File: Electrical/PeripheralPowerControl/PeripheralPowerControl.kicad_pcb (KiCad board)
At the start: 2 copper layers, 40 x 63 mm, 6 parts, among them J1 Conn_01x03, J2 Screw_Terminal_01x02, J3 Conn_01x03

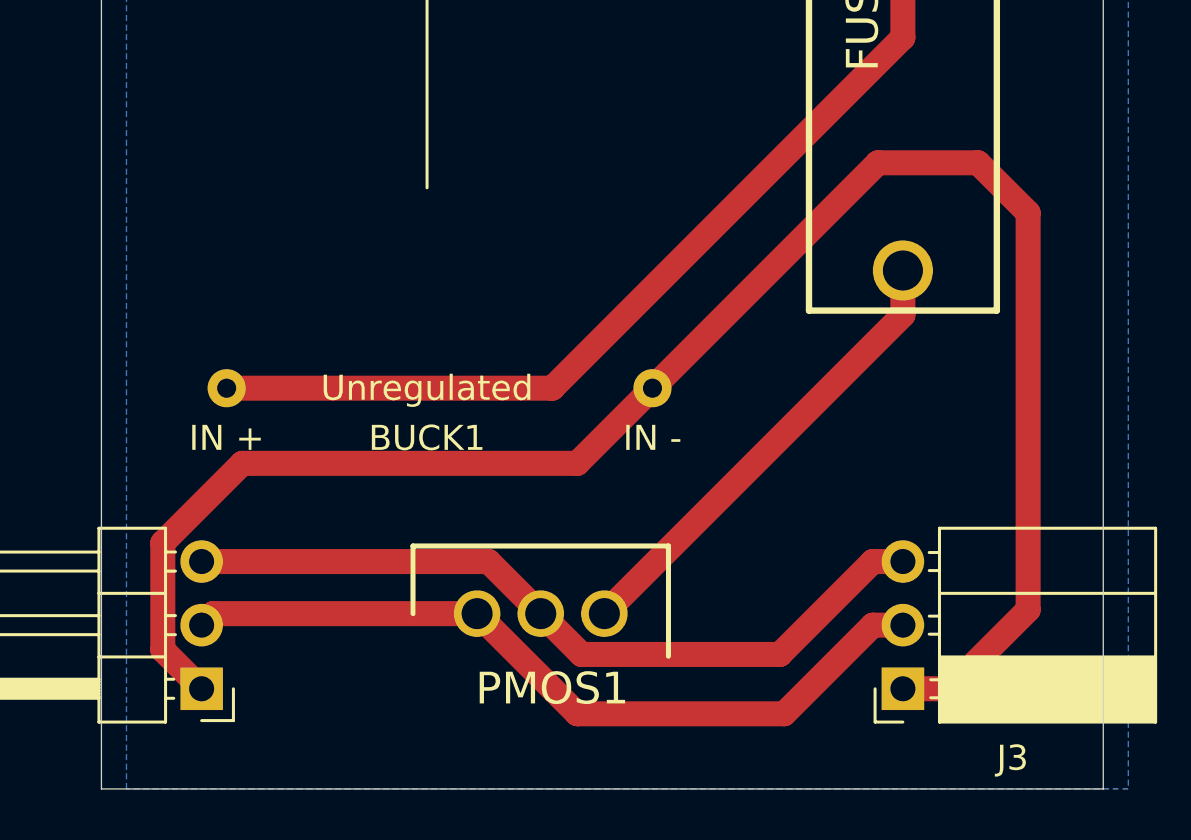
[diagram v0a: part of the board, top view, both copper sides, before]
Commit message: Adds ground plane to the peripheral board
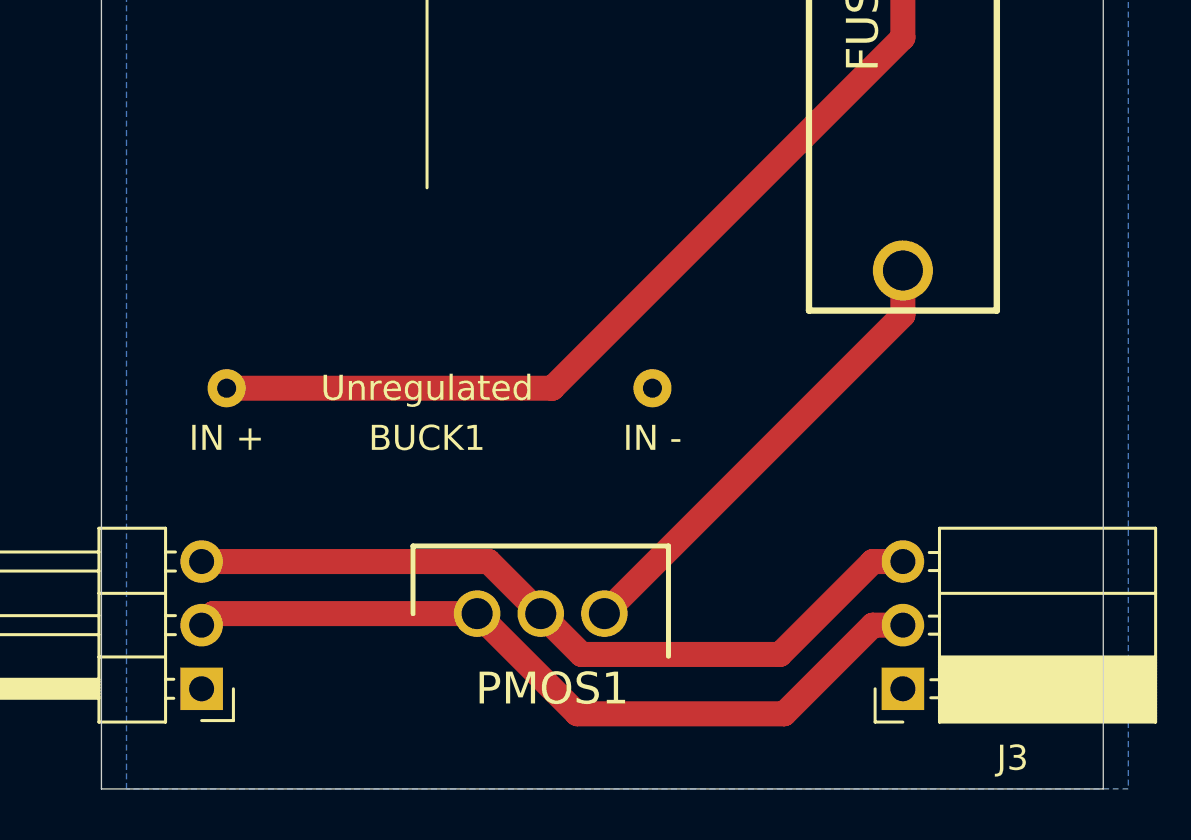
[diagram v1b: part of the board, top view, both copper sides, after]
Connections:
- net Net-(BUCK1-Pad1) renamed GND
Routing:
- net GND: track 70.3 -> 0.00 mm
- added copper zone on B.Cu, net GND
- removed copper zone on B.Cu, net (none)
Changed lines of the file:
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@@
     (thickness 1.6)
     (drawings 6)
-    (tracks 34)
+    (tracks 23)
     (zones 0)
     (modules 6)
@@
   (net 2 "Net-(BUCK1-Pad3)")
   (net 3 "Net-(BUCK1-Pad2)")
-  (net 4 "Net-(BUCK1-Pad1)")
-  (net 5 "Net-(FUSE1-Pad1)")
-  (net 6 "Net-(J1-Pad3)")
-  (net 7 "Net-(J1-Pad2)")
+  (net 4 "Net-(FUSE1-Pad1)")
+  (net 5 "Net-(J1-Pad3)")
+  (net 6 "Net-(J1-Pad2)")
+  (net 7 GND)
   (net_class Default "This is the default net class."
     (clearance 0.2)
@@
     (uvia_dia 0.3)
     (uvia_drill 0.1)
-    (add_net "Net-(BUCK1-Pad1)")
+    (add_net GND)
     (add_net "Net-(BUCK1-Pad2)")
     (add_net "Net-(BUCK1-Pad3)")
@@
     )
     (pad 3 thru_hole circle (at 5.08 0) (size 1.86 1.86) (drill 1.24) (layers *.Cu *.Mask)
-      (net 5 "Net-(FUSE1-Pad1)"))
+      (net 4 "Net-(FUSE1-Pad1)"))
     (pad 2 thru_hole circle (at 2.54 0) (size 1.86 1.86) (drill 1.24) (layers *.Cu *.Mask)
-      (net 6 "Net-(J1-Pad3)"))
+      (net 5 "Net-(J1-Pad3)"))
     (pad 1 thru_hole circle (at 0 0) (size 1.86 1.86) (drill 1.24) (layers *.Cu *.Mask)
-      (net 7 "Net-(J1-Pad2)"))
+      (net 6 "Net-(J1-Pad2)"))
     (model "C:\\Users\\jklei\\KiCad Libs\\SamacSys_Parts.3dshapes\\IPP120P04P4L03AKSA1.stp"
       (at (xyz 0 0 0))
@@
     (fp_line (start -10.03 -1.27) (end -2.49 -1.27) (layer F.Fab) (width 0.1))
     (pad 3 thru_hole oval (at 0 5.08 180) (size 1.7 1.7) (drill 1) (layers *.Cu *.Mask)
-      (net 6 "Net-(J1-Pad3)"))
+      (net 5 "Net-(J1-Pad3)"))
     (pad 2 thru_hole oval (at 0 2.54 180) (size 1.7 1.7) (drill 1) (layers *.Cu *.Mask)
-      (net 7 "Net-(J1-Pad2)"))
+      (net 6 "Net-(J1-Pad2)"))
     (pad 1 thru_hole rect (at 0 0 180) (size 1.7 1.7) (drill 1) (layers *.Cu *.Mask)
-      (net 4 "Net-(BUCK1-Pad1)"))
+      (net 7 GND))
     (model ${KISYS3DMOD}/Connector_PinSocket_2.54mm.3dshapes/PinSocket_1x03_P2.54mm_Horizontal.wrl
       (at (xyz 0 0 0))
@@
     (fp_line (start 2.135 -1.27) (end 4.04 -1.27) (layer F.Fab) (width 0.1))
     (pad 3 thru_hole oval (at 0 5.08 180) (size 1.7 1.7) (drill 1) (layers *.Cu *.Mask)
-      (net 6 "Net-(J1-Pad3)"))
+      (net 5 "Net-(J1-Pad3)"))
     (pad 2 thru_hole oval (at 0 2.54 180) (size 1.7 1.7) (drill 1) (layers *.Cu *.Mask)
-      (net 7 "Net-(J1-Pad2)"))
+      (net 6 "Net-(J1-Pad2)"))
     (pad 1 thru_hole rect (at 0 0 180) (size 1.7 1.7) (drill 1) (layers *.Cu *.Mask)
-      (net 4 "Net-(BUCK1-Pad1)"))
+      (net 7 GND))
     (model ${KISYS3DMOD}/Connector_PinHeader_2.54mm.3dshapes/PinHeader_1x03_P2.54mm_Horizontal.wrl
       (at (xyz 0 0 0))
@@
       (net 3 "Net-(BUCK1-Pad2)"))
     (pad 1 thru_hole circle (at -11.3 0 90) (size 2.4 2.4) (drill 1.6) (layers *.Cu *.Mask)
-      (net 5 "Net-(FUSE1-Pad1)"))
+      (net 4 "Net-(FUSE1-Pad1)"))
   )
   (module SCR_KiCAD_Lib:LM2596 (layer F.Cu)
@@
       (net 3 "Net-(BUCK1-Pad2)"))
     (pad 1 thru_hole circle (at -10 3 180) (size 1.524 1.524) (drill 0.762) (layers *.Cu *.Mask)
-      (net 4 "Net-(BUCK1-Pad1)"))
+      (net 7 GND))
   )
   (gr_line (start 53 10) (end 53 73) (layer Edge.Cuts) (width 0.05))
@@
   (segment (start 31 57) (end 18 57) (width 1) (layer F.Cu) (net 3))
   (segment (start 45 43) (end 31 57) (width 1) (layer F.Cu) (net 3))
-  (segment (start 15.449999 67.449999) (end 17 69) (width 1) (layer F.Cu) (net 4))
-  (segment (start 15.449999 63.175999) (end 15.449999 67.449999) (width 1) (layer F.Cu) (net 4))
-  (segment (start 18.625998 60) (end 15.449999 63.175999) (width 1) (layer F.Cu) (net 4))
-  (segment (start 32 60) (end 18.625998 60) (width 1) (layer F.Cu) (net 4))
-  (segment (start 35 57) (end 32 60) (width 1) (layer F.Cu) (net 4))
-  (segment (start 46.85 69) (end 45 69) (width 1) (layer F.Cu) (net 4))
-  (segment (start 50 65.85) (end 46.85 69) (width 1) (layer F.Cu) (net 4))
-  (segment (start 50 50) (end 50 65.85) (width 1) (layer F.Cu) (net 4))
-  (segment (start 48 48) (end 50 50) (width 1) (layer F.Cu) (net 4))
-  (segment (start 44 48) (end 48 48) (width 1) (layer F.Cu) (net 4))
-  (segment (start 35 57) (end 44 48) (width 1) (layer F.Cu) (net 4))
-  (segment (start 45 54.08) (end 45 52.3) (width 1) (layer F.Cu) (net 5))
-  (segment (start 33.08 66) (end 45 54.08) (width 1) (layer F.Cu) (net 5))
-  (segment (start 28.46 63.92) (end 30.54 66) (width 1) (layer F.Cu) (net 6))
-  (segment (start 17 63.92) (end 28.46 63.92) (width 1) (layer F.Cu) (net 6))
-  (segment (start 43.797919 63.92) (end 45 63.92) (width 1) (layer F.Cu) (net 6))
-  (segment (start 40.087918 67.630001) (end 43.797919 63.92) (width 1) (layer F.Cu) (net 6))
-  (segment (start 32.170001 67.630001) (end 40.087918 67.630001) (width 1) (layer F.Cu) (net 6))
-  (segment (start 30.54 66) (end 32.170001 67.630001) (width 1) (layer F.Cu) (net 6))
-  (segment (start 17.46 66) (end 17 66.46) (width 1) (layer F.Cu) (net 7))
-  (segment (start 28 66) (end 17.46 66) (width 1) (layer F.Cu) (net 7))
-  (segment (start 32 70) (end 28 66) (width 1) (layer F.Cu) (net 7))
-  (segment (start 40.257919 70) (end 32 70) (width 1) (layer F.Cu) (net 7))
-  (segment (start 43.797919 66.46) (end 40.257919 70) (width 1) (layer F.Cu) (net 7))
-  (segment (start 45 66.46) (end 43.797919 66.46) (width 1) (layer F.Cu) (net 7))
-  (zone (net 0) (net_name "") (layer B.Cu) (hatch edge 0.508)
+  (segment (start 45 54.08) (end 45 52.3) (width 1) (layer F.Cu) (net 4))
+  (segment (start 33.08 66) (end 45 54.08) (width 1) (layer F.Cu) (net 4))
+  (segment (start 28.46 63.92) (end 30.54 66) (width 1) (layer F.Cu) (net 5))
+  (segment (start 17 63.92) (end 28.46 63.92) (width 1) (layer F.Cu) (net 5))
+  (segment (start 43.797919 63.92) (end 45 63.92) (width 1) (layer F.Cu) (net 5))
+  (segment (start 40.087918 67.630001) (end 43.797919 63.92) (width 1) (layer F.Cu) (net 5))
+  (segment (start 32.170001 67.630001) (end 40.087918 67.630001) (width 1) (layer F.Cu) (net 5))
+  (segment (start 30.54 66) (end 32.170001 67.630001) (width 1) (layer F.Cu) (net 5))
+  (segment (start 17.46 66) (end 17 66.46) (width 1) (layer F.Cu) (net 6))
+  (segment (start 28 66) (end 17.46 66) (width 1) (layer F.Cu) (net 6))
+  (segment (start 32 70) (end 28 66) (width 1) (layer F.Cu) (net 6))
+  (segment (start 40.257919 70) (end 32 70) (width 1) (layer F.Cu) (net 6))
+  (segment (start 43.797919 66.46) (end 40.257919 70) (width 1) (layer F.Cu) (net 6))
+  (segment (start 45 66.46) (end 43.797919 66.46) (width 1) (layer F.Cu) (net 6))
+  (zone (net 7) (net_name GND) (layer B.Cu) (hatch edge 0.508)
     (connect_pads (clearance 0.508))
     (min_thickness 0.254)

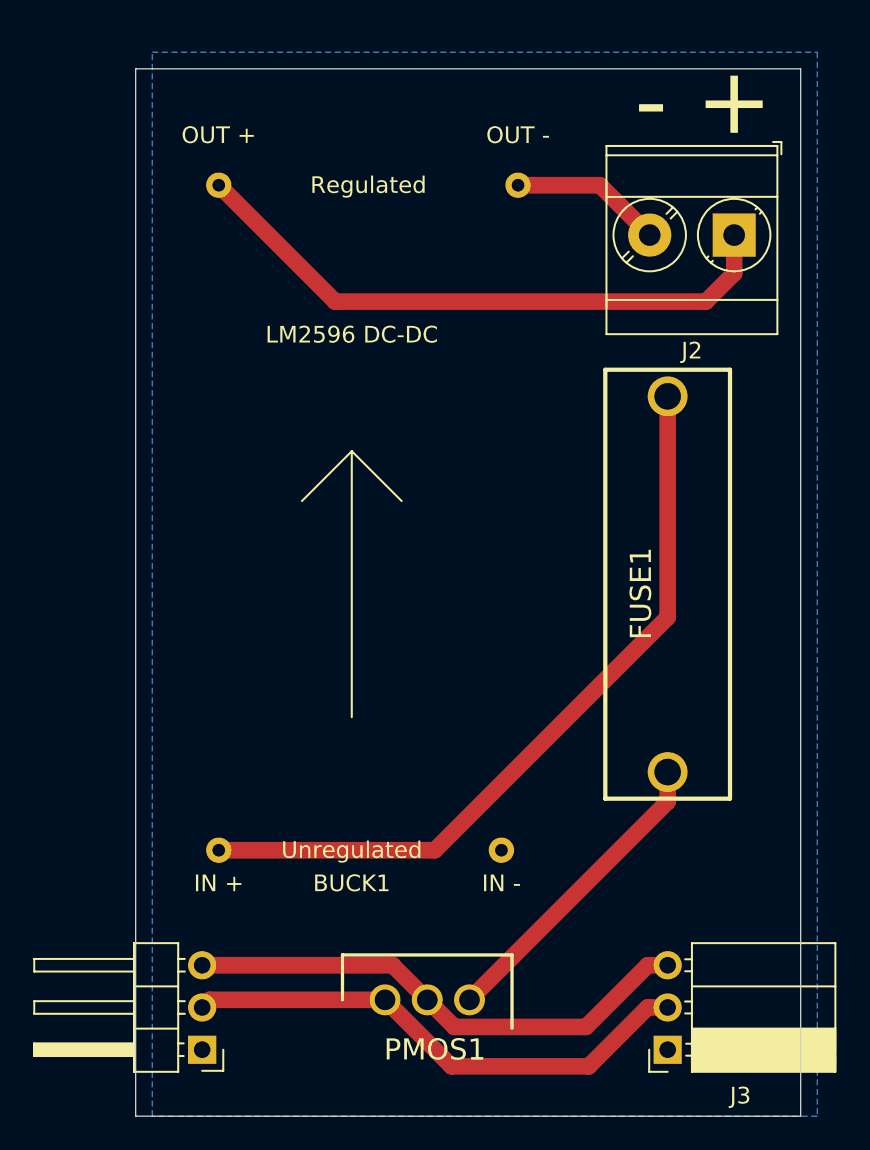
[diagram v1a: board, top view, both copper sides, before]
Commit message: Verified Peripheral and Motor power controllers
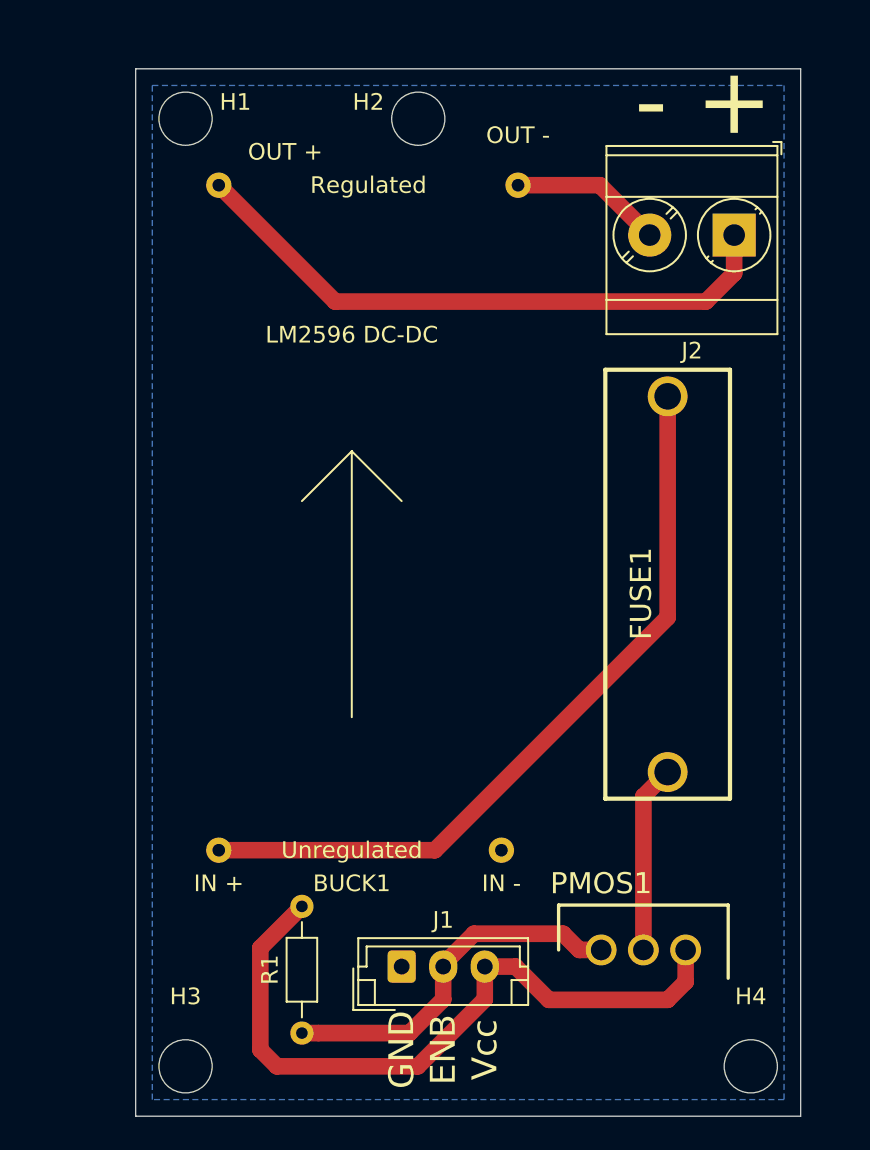
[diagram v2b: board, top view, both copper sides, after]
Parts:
- removed J3: Conn_01x03, Connector_PinSocket_2.54mm:PinSocket_1x03_P2.54mm_Horizontal
- added H1: MountingHole, MountingHole:MountingHole_3.2mm_M3, F.Cu at (16.0, 13.0)
- added H2: MountingHole, MountingHole:MountingHole_3.2mm_M3, F.Cu at (30.0, 13.0)
- added H3: MountingHole, MountingHole:MountingHole_3.2mm_M3, F.Cu at (16.0, 70.0)
- added H4: MountingHole, MountingHole:MountingHole_3.2mm_M3, F.Cu at (50.0, 70.0)
- added R1: R, Resistor_THT:R_Axial_DIN0204_L3.6mm_D1.6mm_P7.62mm_Horizontal, F.Cu at (23.0, 68.0)
- J1: footprint Connector_PinHeader_2.54mm:PinHeader_1x03_P2.54mm_Horizontal -> Connector_JST:JST_EH_B3B-EH-A_1x03_P2.50mm_Vertical
- moved PMOS1 13.3 mm to (41.0, 63.0)
- moved J1 13.0 mm to (29.0, 64.0), turned to 0 degrees
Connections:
- PMOS1 pad 2: Net-(J1-Pad3) -> Net-(FUSE1-Pad1)
- PMOS1 pad 3: Net-(FUSE1-Pad1) -> Net-(J1-Pad3)
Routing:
- net Net-(J1-Pad3): track 31.1 -> 42.5 mm
- net Net-(J1-Pad2): track 31.3 -> 22.1 mm
- net Net-(FUSE1-Pad1): track 18.6 -> 11.3 mm
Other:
- board text added: "ENB"
- board text added: "GND"
- board text added: "Vcc"
